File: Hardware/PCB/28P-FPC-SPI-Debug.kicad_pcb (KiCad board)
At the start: 2 copper layers, 97.4 x 36.8 mm, 40 parts, among them J1 Conn_01x08, J2 Conn_01x24, J3 SFV24R-1STBE1HLF, Q1 Si1308EDL, Q2 AO3401A, Q3 S8050, U1 RT9193-33GB, U2 TXB0108PW

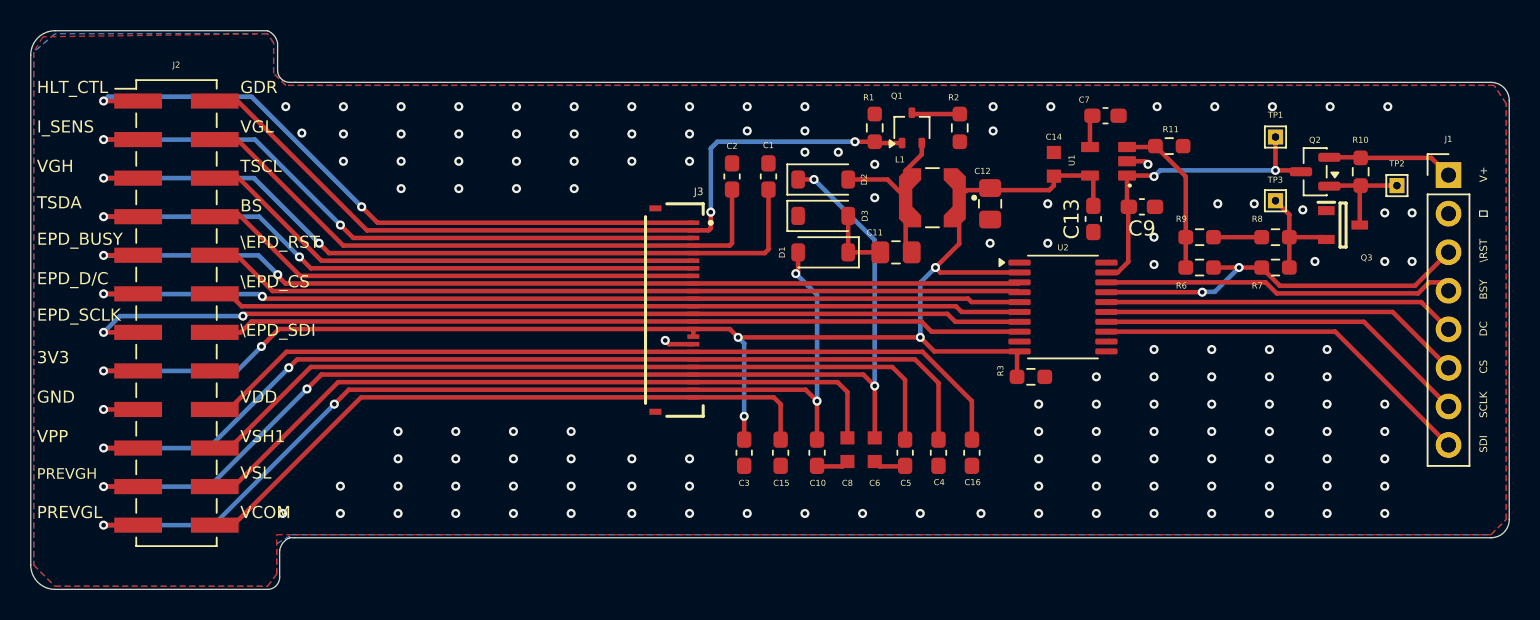
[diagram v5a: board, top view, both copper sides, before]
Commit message: Modified J2 to THT due to parts issue.
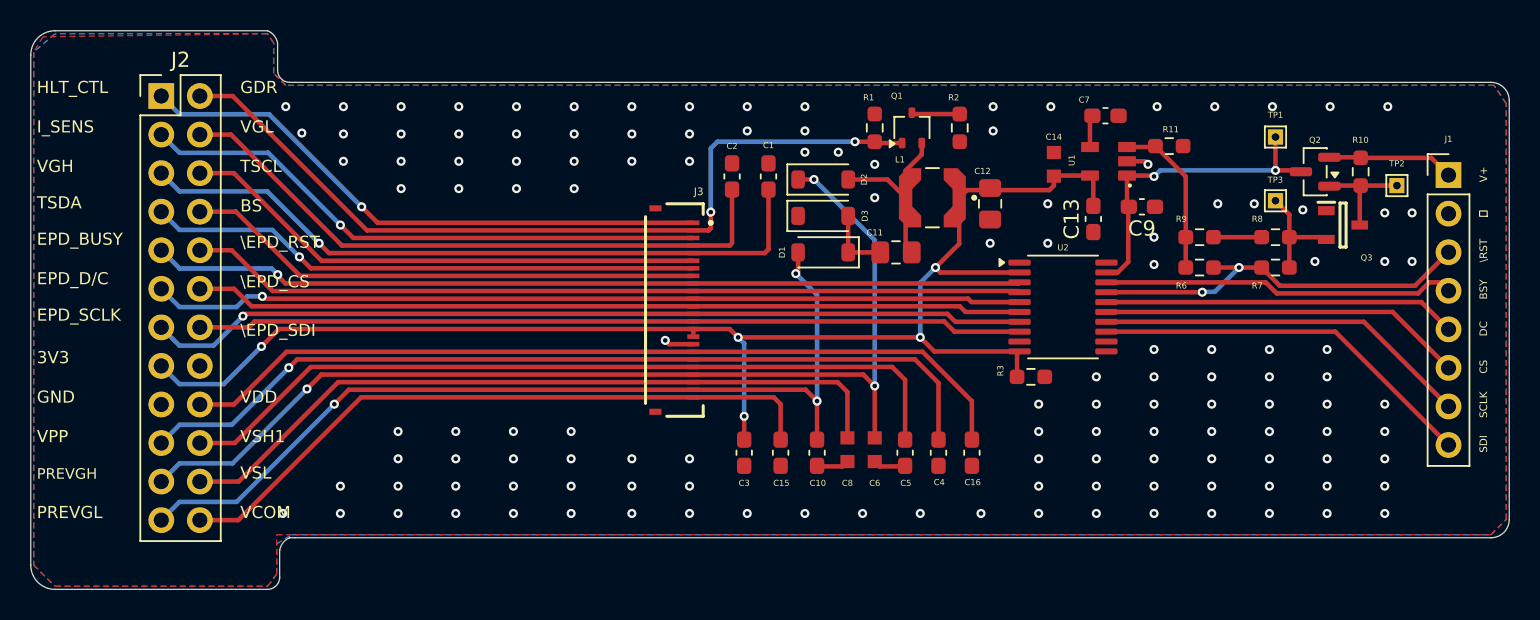
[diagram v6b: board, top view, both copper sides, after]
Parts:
- J2: footprint Connector_PinHeader_2.54mm:PinHeader_2x12_P2.54mm_Vertical_SMD -> Connector_PinHeader_2.54mm:PinHeader_2x12_P2.54mm_Vertical
- moved J2 14.3 mm to (111.2, 45.9)
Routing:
- net /PREVGH: track 76.2 -> 70.0 mm, vias 4 -> 3
- net /VPP: track 64.0 -> 57.8 mm, vias 2 -> 1
- net /PREVGL: track 66.2 -> 60.0 mm, vias 4 -> 3
- net /HLT_CTL: track 44.7 -> 38.5 mm, vias 2 -> 1
- net /EPD_BUSY: track 63.5 -> 57.5 mm, vias 2 -> 1
- net /TSDA: track 42.5 -> 36.6 mm, vias 2 -> 1
- net /CURR_SENSE: track 43.8 -> 37.9 mm, vias 2 -> 1
- net /VGH: track 52.1 -> 46.2 mm, vias 2 -> 1
- net /EPD_D/C: track 62.8 -> 57.3 mm, vias 2 -> 1
- net /EPD_SCLK: track 63.3 -> 57.9 mm, vias 2 -> 1
- net +3V3: track 101.0 -> 95.8 mm, vias 6 -> 5
- net /TSCL: track 32.5 -> 34.9 mm
- net /VCOM: track 41.7 -> 44.1 mm
- net /GDR: track 53.0 -> 55.3 mm
- net /VGL: track 39.3 -> 41.7 mm
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
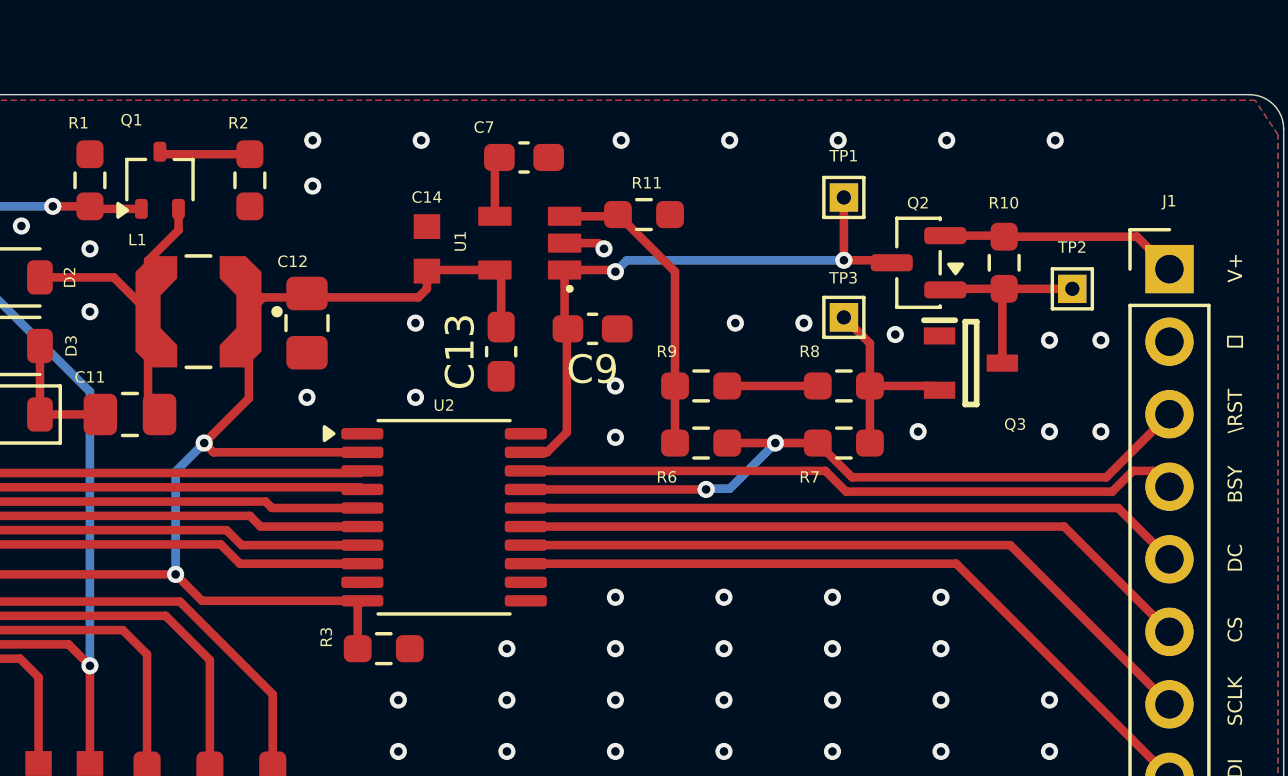
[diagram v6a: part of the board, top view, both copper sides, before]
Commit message: Font size changes on some silkscreen prints. Footprint assignment mods for consistency.
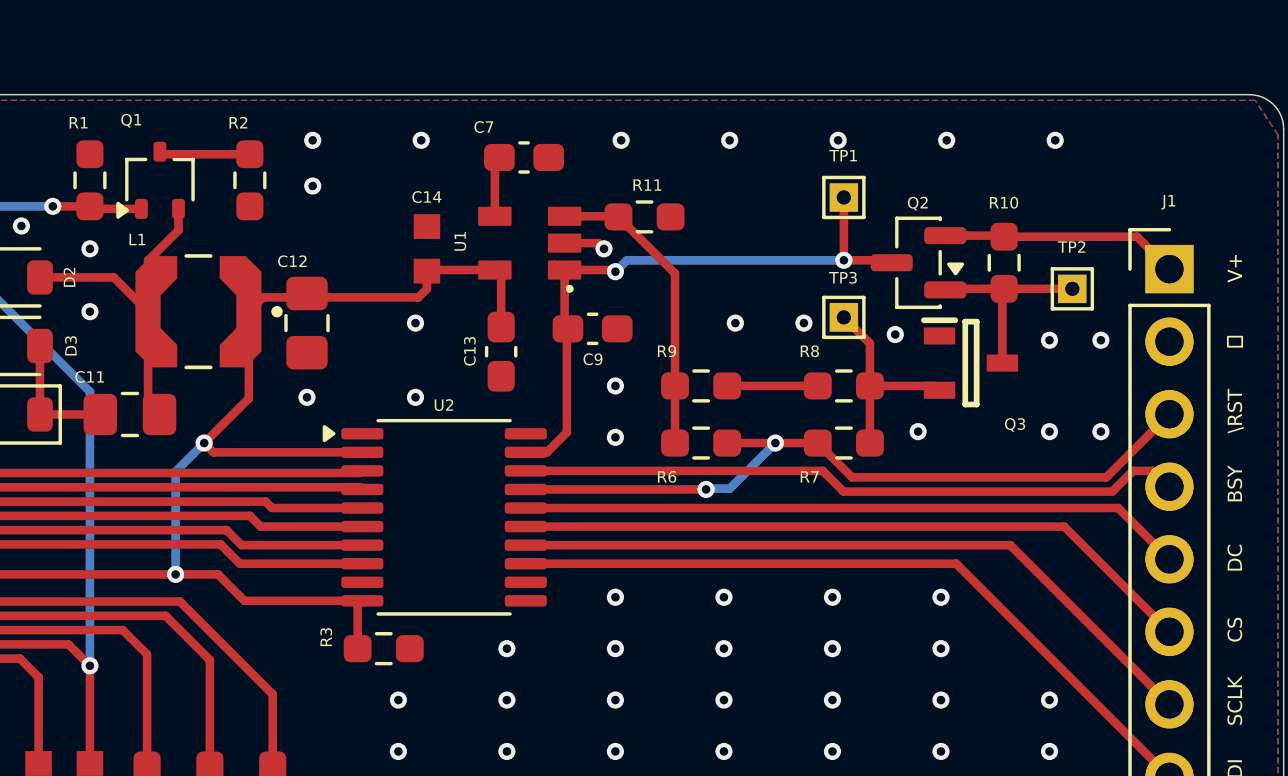
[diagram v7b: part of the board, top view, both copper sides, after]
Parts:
- moved R11 0.08 mm to (177.6, 49.3)
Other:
- board text added: "₍ ^. .^₎ Rev1.2 PROTOTYPE"
- board text removed: "₍ ^. .^₎ Rev1.1 PROTOTYPE"
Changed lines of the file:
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@@
 		(allow_soldermask_bridges_in_footprints no)
 		(tenting front back)
-		(grid_origin 198.8 73.8)
+		(aux_axis_origin 103.06863 77.931371)
+		(grid_origin 103.06863 77.931371)
 		(pcbplotparams
 			(layerselection 0x00000000_00000000_55555555_5755f5ff)
@@
 			(drillshape 0)
 			(scaleselection 1)
-			(outputdirectory "./")
+			(outputdirectory "geber/")
 		)
 	)
@@
 	(footprint "Resistor_SMD:R_0603_1608Metric_Pad0.98x0.95mm_HandSolder"
 		(layer "F.Cu")
-		(at 177.6 49.2)
+		(at 177.61863 49.281371)
 		(descr "Resistor SMD 0603 (1608 Metric), square (rectangular) end terminal, IPC-7351 nominal with elongated pad for handsoldering. (Body size source: IPC-SM-782 page 72, https://www.pcb-3d.com/wordpress/wp-content/uploads/ipc-sm-782a_amendment_1_and_2.pdf), generated with kicad-footprint-generator")
 		(tags "resistor handsolder")
@@
 		(tags "capacitor handsolder")
 		(property "Reference" "C9"
-			(at 0 -1.43 180)
+			(at -0.01863 -1.081371 180)
 			(layer "F.SilkS")
 			(effects
 				(font
-					(size 1 1)
-					(thickness 0.15)
+					(size 0.4 0.4)
+					(thickness 0.05)
 				)
 			)
@@
 		(tags "capacitor handsolder")
 		(property "Reference" "C13"
-			(at 0 -1.43 90)
+			(at 0.018629 -1.08137 90)
 			(layer "F.SilkS")
 			(effects
 				(font
-					(size 1 1)
-					(thickness 0.15)
+					(size 0.4 0.4)
+					(thickness 0.05)
 				)
 			)
@@
 		(layer "F.Cu")
 		(at 156.4 69.2 -90)
+		(descr "CAP CER 1UF 25V X7R 0603")
+		(tags "CAP CER 1UF 25V X7R 0603")
 		(property "Reference" "C8"
 			(at 2.2 0 0)
@@
 		)
 	)
-	(gr_text "₍ ^. .^₎\nRev1.1 PROTOTYPE"
+	(gr_text "₍ ^. .^₎\nRev1.2 PROTOTYPE"
 		(at 190.3 73.7 0)
 		(layer "B.SilkS")
@@
 			(justify left bottom mirror)
 		)
-		(render_cache "₍ ^. .^₎\nRev1.1 PROTOTYPE" 0
+		(render_cache "₍ ^. .^₎\nRev1.2 PROTOTYPE" 0
 			(polygon
 				(pts
@@
 			(polygon
 				(pts
-					(xy 184.377629 73.445) (xy 184.377629 73.22225) (xy 184.036453 73.22225) (xy 184.036453 72.360928)
-					(xy 184.333574 72.524692) (xy 184.415548 72.319528) (xy 183.990382 72.096779) (xy 183.780273 72.096779)
-					(xy 183.780273 73.22225) (xy 183.486174 73.22225) (xy 183.486174 73.445)
+					(xy 184.40126 73.445) (xy 184.40126 73.262459) (xy 184.08463 72.944637) (xy 183.941748 72.791131)
+					(xy 183.8921 72.727392) (xy 183.858674 72.676001) (xy 183.83376 72.625525) (xy 183.820298 72.582395)
+					(xy 183.811047 72.493368) (xy 183.814144 72.456357) (xy 183.82332 72.421469) (xy 183.838555 72.389418)
+					(xy 183.859224 72.362393) (xy 183.885405 72.340254) (xy 183.918667 72.322643) (xy 183.95617 72.311678)
+					(xy 184.000641 72.307805) (xy 184.077006 72.316669) (xy 184.147186 72.342976) (xy 184.212199 72.383381)
+					(xy 184.275231 72.436765) (xy 184.407397 72.265032) (xy 184.314818 72.191497) (xy 184.211209 72.13424)
+					(xy 184.137053 72.10709) (xy 184.058607 72.090644) (xy 183.974995 72.085055) (xy 183.879435 72.091585)
+					(xy 183.796667 72.110151) (xy 183.72157 72.141695) (xy 183.65983 72.18434) (xy 183.609708 72.239114)
+					(xy 183.57172 72.307164) (xy 183.548661 72.384473) (xy 183.540487 72.476974) (xy 183.545996 72.554975)
+					(xy 183.562011 72.625901) (xy 183.588162 72.693528) (xy 183.624568 72.760448) (xy 183.669368 72.824761)
+					(xy 183.725501 72.891423) (xy 183.862247 73.029542) (xy 184.056969 73.216388) (xy 183.49231 73.216388)
+					(xy 183.49231 73.445)
 				)
 			)
@@
 	)
 	(segment
-		(start 196 58.73)
-		(end 195.445 58.175)
+		(start 184.588259 58.901)
+		(end 183.862259 58.175)
 		(width 0.3)
 		(layer "F.Cu")
@@
 	)
 	(segment
-		(start 193.99752 58.901)
-		(end 184.679979 58.901)
+		(start 194.72352 58.175)
+		(end 193.99752 58.901)
 		(width 0.3)
 		(layer "F.Cu")
@@
 	)
 	(segment
-		(start 184.679979 58.901)
-		(end 183.95398 58.175)
+		(start 195.445 58.175)
+		(end 194.72352 58.175)
 		(width 0.3)
 		(layer "F.Cu")
@@
 	)
 	(segment
-		(start 183.95398 58.175)
+		(start 183.862259 58.175)
 		(end 173.4625 58.175)
 		(width 0.3)
@@
 	)
 	(segment
-		(start 195.445 58.175)
-		(end 194.72352 58.175)
+		(start 196 58.73)
+		(end 195.445 58.175)
 		(width 0.3)
 		(layer "F.Cu")
@@
 	)
 	(segment
-		(start 194.72352 58.175)
-		(end 193.99752 58.901)
+		(start 193.99752 58.901)
+		(end 184.588259 58.901)
 		(width 0.3)
 		(layer "F.Cu")
@@
 	)
 	(segment
+		(start 161.2 61.8)
+		(end 162.687259 61.8)
+		(width 0.3)
+		(layer "F.Cu")
+		(net 19)
+	)
+	(segment
 		(start 146.25 61.75)
 		(end 146.25 61.25)
@@
 	)
 	(segment
-		(start 162.125 62.725)
-		(end 167.7375 62.725)
+		(start 162.687259 61.8)
+		(end 163.612259 62.725)
 		(width 0.3)
 		(layer "F.Cu")
@@
 	)
 	(segment
-		(start 172.38 51.14)
-		(end 170.04 51.14)
+		(start 163.612259 62.725)
+		(end 167.7375 62.725)
 		(width 0.3)
 		(layer "F.Cu")
@@
 	)
 	(segment
-		(start 161.2 61.8)
-		(end 162.125 62.725)
+		(start 172.38 51.14)
+		(end 170.04 51.14)
 		(width 0.3)
 		(layer "F.Cu")
@@
 	)
 	(segment
-		(start 178.6875 51.2)
-		(end 176.6875 49.2)
+		(start 176.70613 49.281371)
+		(end 178.6875 51.262741)
+		(width 0.3)
+		(layer "F.Cu")
+		(net 33)
+	)
+	(segment
+		(start 178.6875 51.262741)
+		(end 178.6875 55.2)
 		(width 0.3)
 		(layer "F.Cu")
@@
 	(segment
 		(start 174.82 49.26)
-		(end 176.6275 49.26)
+		(end 176.684759 49.26)
 		(width 0.3)
 		(layer "F.Cu")
@@
 	)
 	(segment
-		(start 178.6875 55.2)
-		(end 178.6875 51.2)
+		(start 176.684759 49.26)
+		(end 176.70613 49.281371)
 		(width 0.3)
 		(layer "F.Cu")
